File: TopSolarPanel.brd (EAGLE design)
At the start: 81 x 81 mm, 18 parts

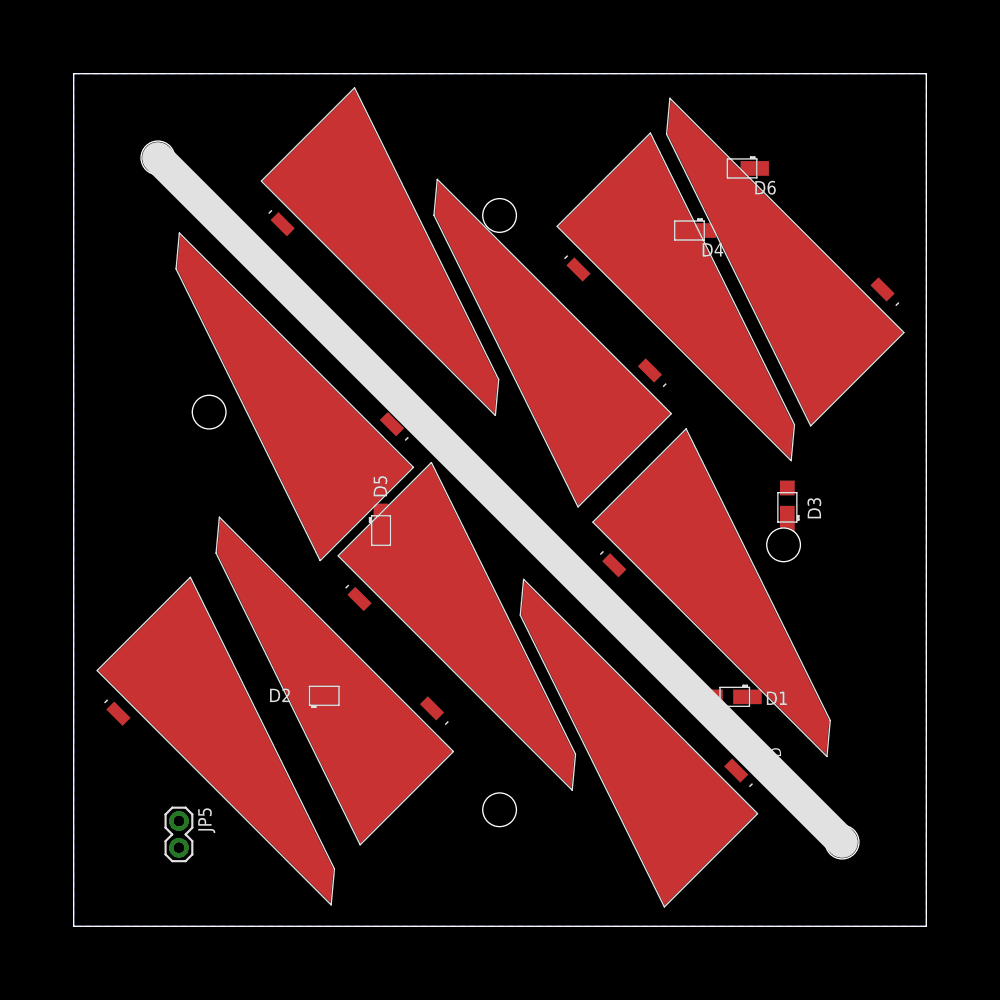
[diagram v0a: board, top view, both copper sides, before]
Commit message: Fixed solar cell footprints
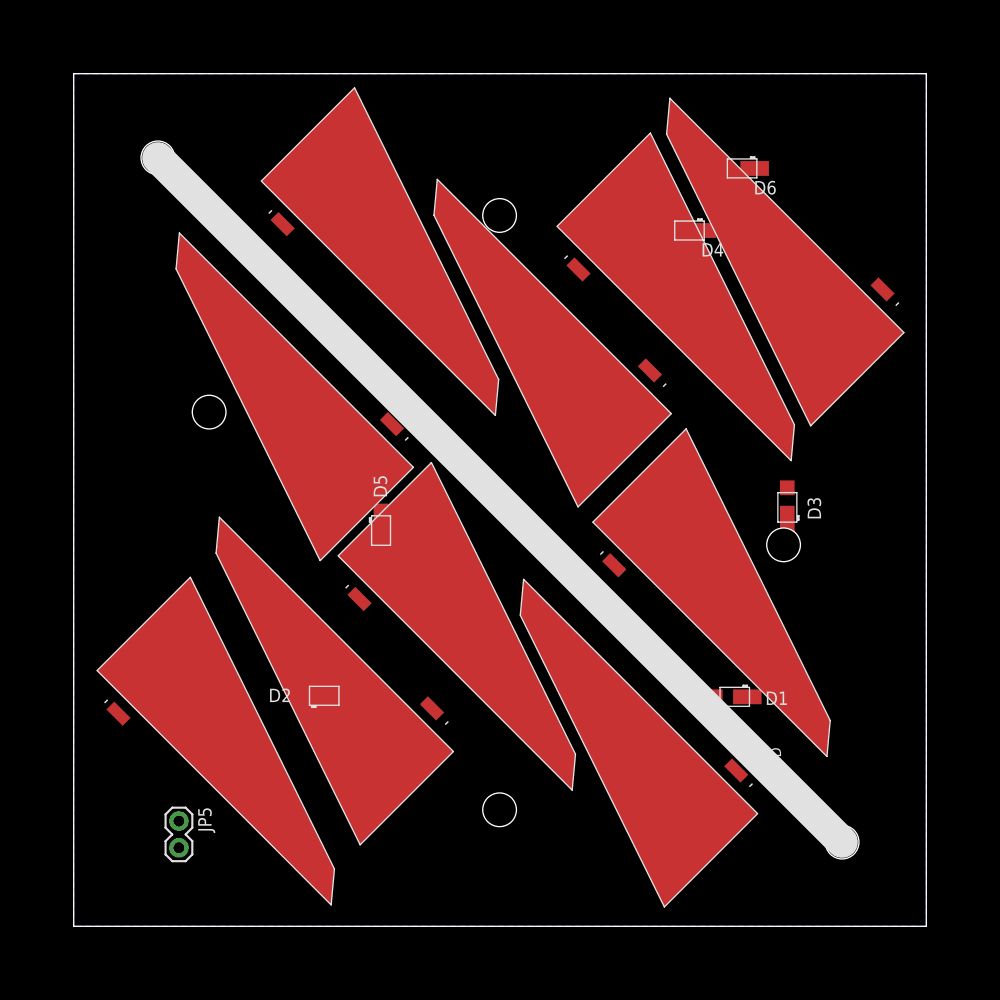
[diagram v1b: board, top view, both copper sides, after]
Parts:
- D1, D2, D3, D4, D5, D6: device phonesat:SB_DIODE -> Solar:SB_DIODE
- SL1, SL10, SL2, SL3, SL4, SL5, SL6, SL7, SL8, SL9: device phonesat:SOLAR_CELL -> Solar:SOLAR_CELL
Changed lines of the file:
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@@
 </class>
 </classes>
-<designrules name="SSC-EAGLE-2Lyr_v1.0.0.3">
-<description language="en">&lt;b&gt;EAGLE Design Rules for *2* Layer Designs (DS)&lt;/b&gt;
+<designrules name="OSHPark-2layer">
+<description language="de">&lt;b&gt;EAGLE Design Rules&lt;/b&gt;
 &lt;p&gt;
-This Sunstone Circuits 2 Layer .DRU has been set to cover our minimum requirements for our double sided products. For questions, comments, suggestions, please contact Sunstone Customer Support: &lt;p&gt;&lt;b&gt;Email:&lt;/b&gt;  mailto:support@sunstone.com&lt;br&gt;&lt;b&gt;Phone:&lt;/b&gt; 800-228-8198.&lt;p&gt; v1.1Mod10/16/07~Layers-core reversal.Distance C/D.Restring%.Supply G%.&lt;p&gt; v1.2 Mod12/06/07~Distance C/D to 20mils.&lt;p&gt;v1.3Mod12/12/07~Supply/Annulus Value to 12.5mils&lt;p&gt;1/15/08 SSC-EAGLE-2Lyr_v1.0.0.3~For Release&lt;p&gt;10/3/08 Description Edit.&lt;p&gt;
+Die Standard-Design-Rules sind so gewählt, dass sie für
+die meisten Anwendungen passen. Sollte ihre Platine
+besondere Anforderungen haben, treffen Sie die erforderlichen
+Einstellungen hier und speichern die Design Rules unter
+einem neuen Namen ab.</description>
+<description language="en">&lt;b&gt;Laen's PCB Order Design Rules&lt;/b&gt;
 &lt;p&gt;
-&lt;i&gt;Attention: Upon running the design check and making modifications, please remember to save any changes before closing the application and sending in your board file to Sunstone Circuits for conversion.&lt;i&gt;</description>
+Please make sure your boards conform to these design rules.</description>
 <param name="layerSetup" value="(1*16)"/>
-<param name="mtCopper" value="0.0178mm 0.0356mm 0.0356mm 0.0356mm 0.0356mm 0.0356mm 0.0356mm 0.0356mm 0.0356mm 0.0356mm 0.0356mm 0.0356mm 0.0356mm 0.0356mm 0.0356mm 0.0178mm"/>
-<param name="mtIsolate" value="59mil 0.1499mm 0.2007mm 0.1499mm 0.2007mm 0.1499mm 0.2007mm 0.1499mm 0.2007mm 0.1499mm 0.2007mm 0.1499mm 0.2007mm 0.1499mm 0.2007mm"/>
+<param name="mtCopper" value="0.0356mm 0.0356mm 0.0356mm 0.0356mm 0.0356mm 0.0356mm 0.0356mm 0.0356mm 0.0356mm 0.0356mm 0.0356mm 0.0356mm 0.0356mm 0.0356mm 0.0356mm 0.0356mm"/>
+<param name="mtIsolate" value="1.5011mm 0.1499mm 0.2007mm 0.1499mm 0.2007mm 0.1499mm 0.2007mm 0.1499mm 0.2007mm 0.1499mm 0.2007mm 0.1499mm 0.2007mm 0.1499mm 0.2007mm"/>
 <param name="mdWireWire" value="6mil"/>
 <param name="mdWirePad" value="6mil"/>
@@
 <param name="mdViaViaSameLayer" value="8mil"/>
 <param name="mnLayersViaInSmd" value="2"/>
-<param name="mdCopperDimension" value="20mil"/>
-<param name="mdDrill" value="16mil"/>
+<param name="mdCopperDimension" value="15mil"/>
+<param name="mdDrill" value="6mil"/>
 <param name="mdSmdStop" value="0mil"/>
 <param name="msWidth" value="6mil"/>
-<param name="msDrill" value="14mil"/>
-<param name="msMicroVia" value="9.9898mm"/>
+<param name="msDrill" value="13mil"/>
+<param name="msMicroVia" value="13mil"/>
 <param name="msBlindViaRatio" value="0.5"/>
 <param name="rvPadTop" value="0.25"/>
@@
 <param name="rvMicroViaOuter" value="0.25"/>
 <param name="rvMicroViaInner" value="0.25"/>
-<param name="rlMinPadTop" value="8mil"/>
-<param name="rlMaxPadTop" value="999mil"/>
-<param name="rlMinPadInner" value="0mil"/>
-<param name="rlMaxPadInner" value="0mil"/>
-<param name="rlMinPadBottom" value="8mil"/>
-<param name="rlMaxPadBottom" value="999mil"/>
-<param name="rlMinViaOuter" value="8mil"/>
-<param name="rlMaxViaOuter" value="999mil"/>
-<param name="rlMinViaInner" value="0mil"/>
-<param name="rlMaxViaInner" value="0mil"/>
-<param name="rlMinMicroViaOuter" value="8mil"/>
-<param name="rlMaxMicroViaOuter" value="999mil"/>
-<param name="rlMinMicroViaInner" value="0mil"/>
-<param name="rlMaxMicroViaInner" value="0mil"/>
+<param name="rlMinPadTop" value="7mil"/>
+<param name="rlMaxPadTop" value="20mil"/>
+<param name="rlMinPadInner" value="7mil"/>
+<param name="rlMaxPadInner" value="20mil"/>
+<param name="rlMinPadBottom" value="7mil"/>
+<param name="rlMaxPadBottom" value="20mil"/>
+<param name="rlMinViaOuter" value="7mil"/>
+<param name="rlMaxViaOuter" value="20mil"/>
+<param name="rlMinViaInner" value="7mil"/>
+<param name="rlMaxViaInner" value="20mil"/>
+<param name="rlMinMicroViaOuter" value="4mil"/>
+<param name="rlMaxMicroViaOuter" value="20mil"/>
+<param name="rlMinMicroViaInner" value="4mil"/>
+<param name="rlMaxMicroViaInner" value="20mil"/>
 <param name="psTop" value="-1"/>
 <param name="psBottom" value="-1"/>
@@
 <param name="mvStopFrame" value="1"/>
 <param name="mvCreamFrame" value="0"/>
-<param name="mlMinStopFrame" value="3mil"/>
-<param name="mlMaxStopFrame" value="3mil"/>
+<param name="mlMinStopFrame" value="4mil"/>
+<param name="mlMaxStopFrame" value="4mil"/>
 <param name="mlMinCreamFrame" value="0mil"/>
 <param name="mlMaxCreamFrame" value="0mil"/>
@@
 <param name="checkRestrict" value="1"/>
 <param name="useDiameter" value="13"/>
-<param name="maxErrors" value="500"/>
+<param name="maxErrors" value="50"/>
 </designrules>
 <autorouter>
@@
 </autorouter>
 <elements>
-<element name="SL3" library="phonesat" package="SOLAR_CELL" value="SOLAR_CELL" x="59.7" y="15.8" rot="R225"/>
-<element name="D2" library="phonesat" package="SB_DIODE" value="SB_DIODE" x="23.8" y="21.9" smashed="yes">
+<element name="SL3" library="Solar" package="SOLAR_CELL" value="SOLAR_CELL" x="59.7" y="15.8" rot="R225"/>
+<element name="D2" library="Solar" package="SB_DIODE" value="SB_DIODE" x="23.8" y="21.9" smashed="yes">
 <attribute name="NAME" x="18.5" y="21.3" size="1.27" layer="25"/>
 </element>
-<element name="SL5" library="phonesat" package="SOLAR_CELL" value="SOLAR_CELL" x="27" y="48.7" rot="R225"/>
-<element name="SL1" library="phonesat" package="SOLAR_CELL" value="SOLAR_CELL" x="30.8" y="21.7" rot="R225"/>
-<element name="SL7" library="phonesat" package="SOLAR_CELL" value="SOLAR_CELL" x="51.5" y="53.8" rot="R225"/>
-<element name="SL10" library="phonesat" package="SOLAR_CELL" value="SOLAR_CELL" x="73.6" y="61.5" rot="R225"/>
-<element name="SL6" library="phonesat" package="SOLAR_CELL" value="SOLAR_CELL" x="23.1" y="65.7" rot="R45"/>
-<element name="SL4" library="phonesat" package="SOLAR_CELL" value="SOLAR_CELL" x="30.4" y="30.1" rot="R45"/>
-<element name="SL8" library="phonesat" package="SOLAR_CELL" value="SOLAR_CELL" x="54.6" y="33.3" rot="R45"/>
-<element name="SL9" library="phonesat" package="SOLAR_CELL" value="SOLAR_CELL" x="51.2" y="61.4" rot="R45"/>
-<element name="SL2" library="phonesat" package="SOLAR_CELL" value="SOLAR_CELL" x="7.5" y="19.2" rot="R45"/>
-<element name="D1" library="phonesat" package="SB_DIODE" value="SB_DIODE" x="62.8" y="21.8" smashed="yes" rot="R180">
+<element name="SL5" library="Solar" package="SOLAR_CELL" value="SOLAR_CELL" x="27" y="48.7" rot="R225"/>
+<element name="SL1" library="Solar" package="SOLAR_CELL" value="SOLAR_CELL" x="30.8" y="21.7" rot="R225"/>
+<element name="SL7" library="Solar" package="SOLAR_CELL" value="SOLAR_CELL" x="51.5" y="53.8" rot="R225"/>
+<element name="SL10" library="Solar" package="SOLAR_CELL" value="SOLAR_CELL" x="73.6" y="61.5" rot="R225"/>
+<element name="SL6" library="Solar" package="SOLAR_CELL" value="SOLAR_CELL" x="23.1" y="65.7" rot="R45"/>
+<element name="SL4" library="Solar" package="SOLAR_CELL" value="SOLAR_CELL" x="30.4" y="30.1" rot="R45"/>
+<element name="SL8" library="Solar" package="SOLAR_CELL" value="SOLAR_CELL" x="54.6" y="33.3" rot="R45"/>
+<element name="SL9" library="Solar" package="SOLAR_CELL" value="SOLAR_CELL" x="51.2" y="61.4" rot="R45"/>
+<element name="SL2" library="Solar" package="SOLAR_CELL" value="SOLAR_CELL" x="7.5" y="19.2" rot="R45"/>
+<element name="D1" library="Solar" package="SB_DIODE" value="SB_DIODE" x="62.8" y="21.8" smashed="yes" rot="R180">
 <attribute name="NAME" x="67.9" y="22.3" size="1.27" layer="25" rot="R180"/>
 </element>
-<element name="D3" library="phonesat" package="SB_DIODE" value="SB_DIODE" x="67.8" y="39.8" smashed="yes" rot="R90">
+<element name="D3" library="Solar" package="SB_DIODE" value="SB_DIODE" x="67.8" y="39.8" smashed="yes" rot="R90">
 <attribute name="NAME" x="71" y="38.6" size="1.27" layer="25" rot="R90"/>
 </element>
-<element name="D4" library="phonesat" package="SB_DIODE" value="SB_DIODE" x="58.5" y="66.1" rot="R180"/>
-<element name="D5" library="phonesat" package="SB_DIODE" value="SB_DIODE" x="29.2" y="37.6" smashed="yes" rot="R270">
+<element name="D4" library="Solar" package="SB_DIODE" value="SB_DIODE" x="58.5" y="66.1" rot="R180"/>
+<element name="D5" library="Solar" package="SB_DIODE" value="SB_DIODE" x="29.2" y="37.6" smashed="yes" rot="R270">
 <attribute name="NAME" x="28.5" y="42.9" size="1.27" layer="25" rot="R270"/>
 </element>
-<element name="D6" library="phonesat" package="SB_DIODE" value="SB_DIODE" x="63.5" y="72" rot="R180"/>
+<element name="D6" library="Solar" package="SB_DIODE" value="SB_DIODE" x="63.5" y="72" rot="R180"/>
 <element name="FRAME1" library="SparkFun-Aesthetics" package="CREATIVE_COMMONS" value="FRAME-LETTER" x="20" y="-13.1" smashed="yes"/>
 <element name="JP5" library="SparkFun-Connectors" package="1X02" value="M02PTH" x="10" y="10" rot="R270"/>

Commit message: New top solar panel
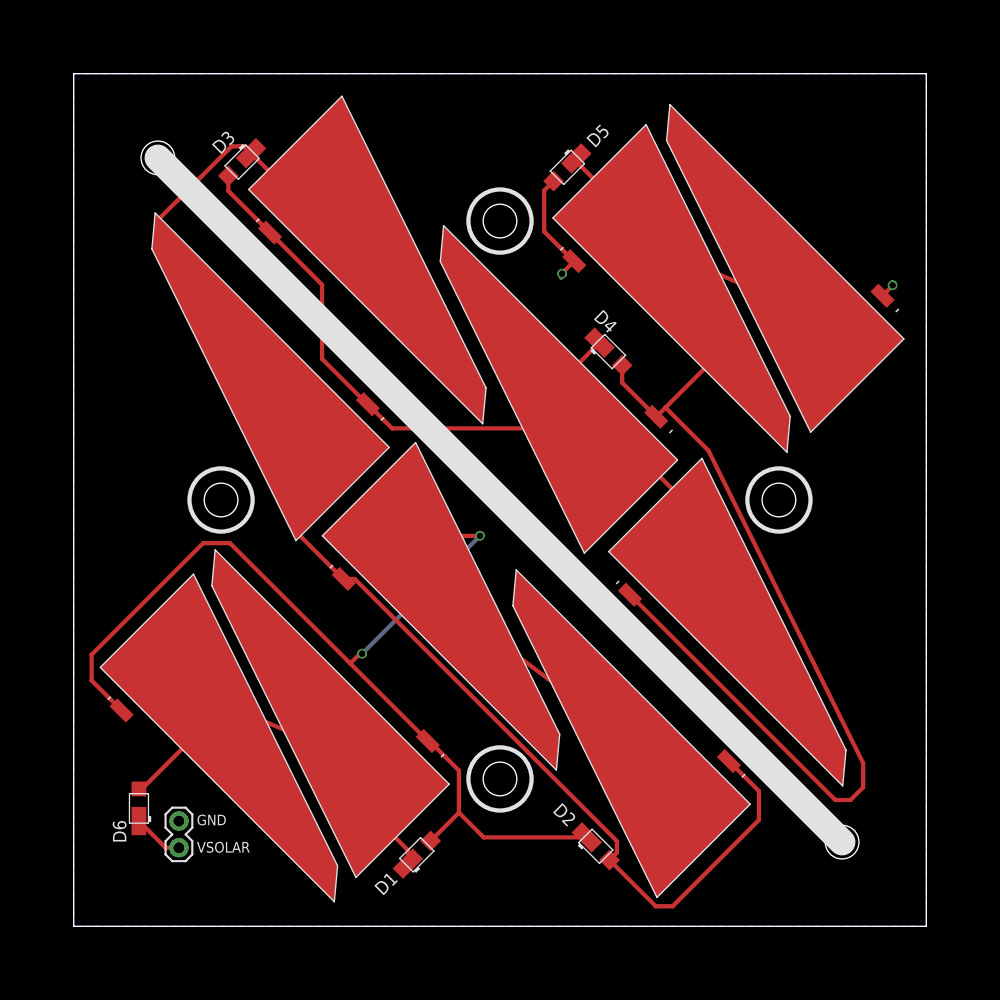
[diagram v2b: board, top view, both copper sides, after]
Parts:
- added U$1: KICKSAT_LOGO, KickSat-Logo:KICKSAT_LOGO
- moved D6 83.5 mm to (6.20, 11.2), turned to 90 degrees
- moved D3 61.3 mm to (16.0, 72.6), turned to 225 degrees
- moved D5 38.8 mm to (46.9, 72.1), turned to 225 degrees
- moved D1 33.7 mm to (32.6, 6.80), turned to 45 degrees
- moved D2 29.5 mm to (49.6, 7.60), turned to 315 degrees
- moved D4 13.8 mm to (50.8, 54.6), turned to 315 degrees
- moved SL7 4.44 mm to (52.1, 49.4)
- moved SL8 3.18 mm to (56.1, 30.5)
- moved SL1 3.13 mm to (30.4, 18.6)
- moved SL5 2.98 mm to (24.7, 50.6)
- moved SL4 2.42 mm to (28.9, 32.0)
- moved SL6 1.44 mm to (21.9, 64.9)
- moved SL3 1.14 mm to (59.0, 16.7)
- moved SL9 0.89 mm to (50.8, 62.2)
- moved SL10 0.60 mm to (73.6, 60.9)
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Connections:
- net GND: now also JP5.1; no longer JP5.2
- net VSOLAR: now also JP5.2; no longer JP5.1
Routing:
- net N$45: track 0.00 -> 147.3 mm, vias 0 -> 2
- net N$50: track 0.00 -> 133.1 mm
- net N$37: track 0.00 -> 127.5 mm
- net N$39: track 0.00 -> 76.6 mm
- net N$9: track 0.00 -> 57.5 mm
- net GND: track 0.00 -> 13.0 mm, vias 0 -> 2
- net VSOLAR: track 0.00 -> 4.85 mm
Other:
- board text added: "VSOLAR"
